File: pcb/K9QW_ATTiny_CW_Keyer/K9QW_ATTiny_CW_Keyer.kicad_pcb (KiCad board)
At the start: 2 copper layers, 13 x 1.4 mm, 25 parts, among them J1 Paddle Input, J2 Key Output, J3 Command, J4 Key LED, J5 Barrel_Jack_MountingPin, J6 Power Input, J7 Paddle Input, J8 Key Output, Q1 MMBT3904, Q2 MMBT3904, SW1 Command, SW2 Power Switch, U1 ATtiny85-20P, U2 LD1117S33TR_SOT223

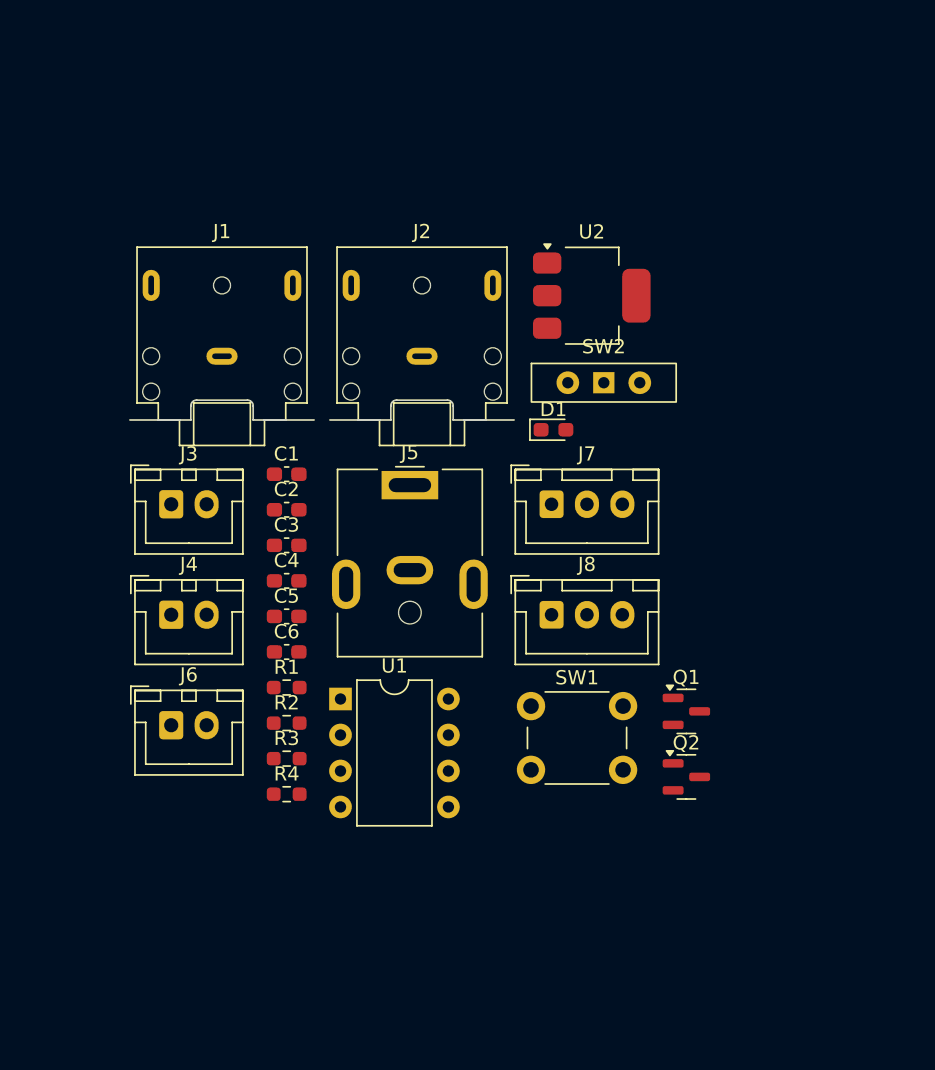
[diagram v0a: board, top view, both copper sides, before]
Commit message: Fixing LED and adding Sidetone Connector
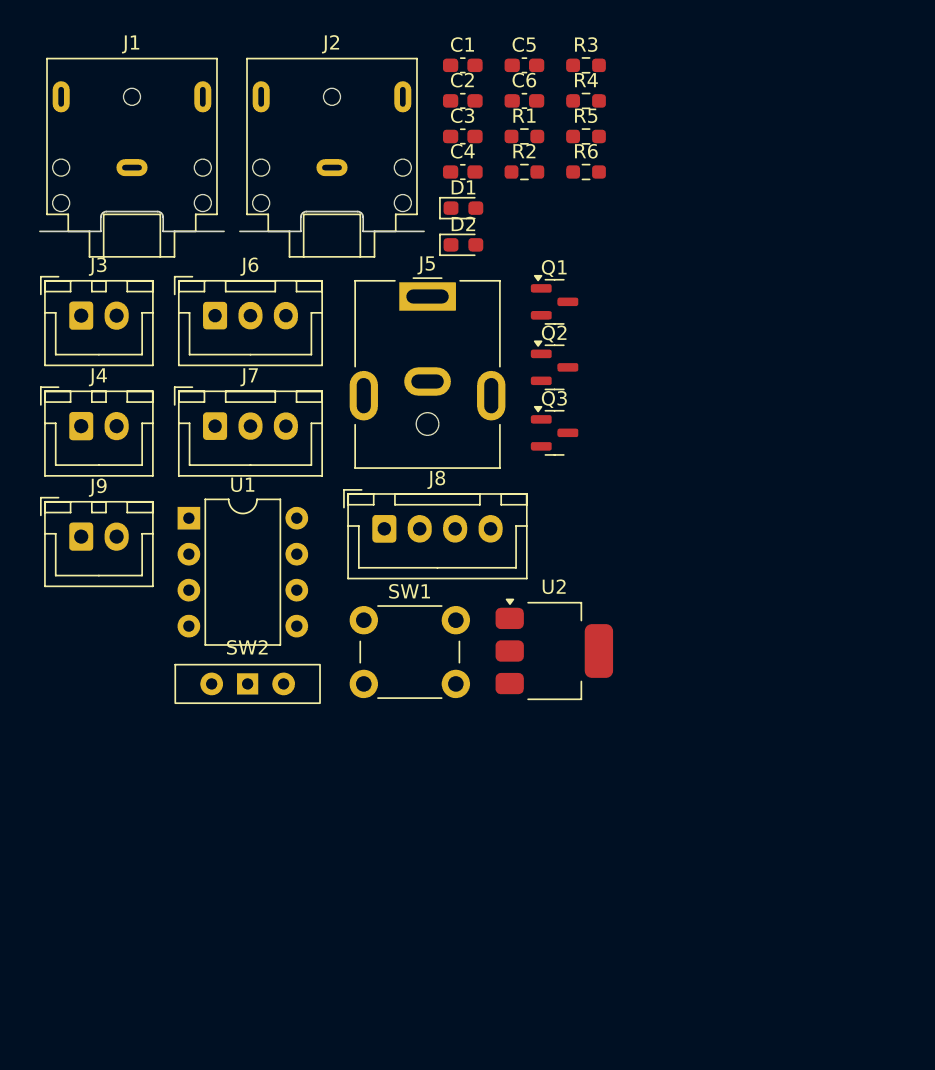
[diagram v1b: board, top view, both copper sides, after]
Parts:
- added D2: Side LED, LED_SMD:LED_0603_1608Metric_Pad1.05x0.95mm_HandSolder, F.Cu at (148.2, 75.0)
- added J9: Power Input, Connector_JST:JST_XH_B2B-XH-A_1x02_P2.50mm_Vertical, F.Cu at (121.2, 95.6)
- added Q3: MMBT3904, Package_TO_SOT_SMD:SOT-23, F.Cu at (154.6, 88.2)
- added R5: 4.7k, Resistor_SMD:R_0603_1608Metric_Pad0.98x0.95mm_HandSolder, F.Cu at (156.8, 67.3)
- added R6: 220, Resistor_SMD:R_0603_1608Metric_Pad0.98x0.95mm_HandSolder, F.Cu at (156.8, 69.8)
- D1: value KEY LED -> LED
- J4: value Key LED -> Sidetone
- J6: value Power Input -> Paddle Input; footprint Connector_JST:JST_XH_B2B-XH-A_1x02_P2.50mm_Vertical -> Connector_JST:JST_XH_B3B-XH-A_1x03_P2.50mm_Vertical
- J7: value Paddle Input -> Key Output
- J8: value Key Output -> LED; footprint Connector_JST:JST_XH_B3B-XH-A_1x03_P2.50mm_Vertical -> Connector_JST:JST_XH_B4B-XH-A_1x04_P2.50mm_Vertical
- Q1: value MMBT3904 -> MMBT2222A
- R3: value 220 -> 4.7k
- R4: value 4.7k -> 220
- moved R4 53.3 mm to (156.8, 64.8)
- moved R3 53.3 mm to (156.8, 62.3)
- moved C6 42.4 mm to (152.5, 64.8)
- moved R1 42.4 mm to (152.5, 67.3)
- moved R2 42.4 mm to (152.5, 69.8)
- moved C5 42.4 mm to (152.5, 62.3)
- moved SW2 32.9 mm to (132.9, 106.0)
- moved C1 31.4 mm to (148.1, 62.3)
- moved C2 31.4 mm to (148.1, 64.8)
- moved C4 31.4 mm to (148.1, 69.8)
- moved C3 31.4 mm to (148.1, 67.3)
- moved Q1 30.4 mm to (154.6, 79.0)
- moved Q2 30.4 mm to (154.6, 83.6)
- moved J6 29.1 mm to (130.6, 80.0)
- moved U2 25.2 mm to (154.6, 103.6)
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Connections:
- D1 pad 1: GND -> Net-(D1-K)
- J4 pad 1: Net-(D1-A) -> SIDETONE
- J6 pad 1: VDC -> GND
- J6 pad 2: GND -> DAH
- J7 pad 2: DAH -> KEY Ring
- J7 pad 3: DIT -> KEY Out
- J8 pad 1: GND -> Net-(D1-A)
- J8 pad 2: KEY Ring -> Net-(D1-K)
- J8 pad 3: KEY Out -> Net-(D2-A)
- Q2 pad 2: Net-(Q2-E) -> GND
- Q2 pad 3: VCC -> Net-(D1-K)
- R3 pad 1: Net-(D1-A) -> KEY
- R3 pad 2: Net-(Q2-E) -> Net-(Q2-B)
- R4 pad 1: KEY -> VCC
- R4 pad 2: Net-(Q2-B) -> Net-(D1-A)

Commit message: Rough PCB Layout
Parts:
- D1: value LED -> Key
- D2: value Side LED -> Sidetone
- moved R3 63.0 mm to (144.1, 124.0), turned to -90 degrees
- moved R5 53.4 mm to (144.1, 119.1), turned to -90 degrees
- moved R4 51.2 mm to (166.2, 115.2), turned to 180 degrees
- moved C1 50.7 mm to (147.4, 113.0)
- moved J1 50.7 mm to (170.5, 91.4), turned to 90 degrees
- moved D2 48.7 mm to (172.5, 117.2), turned to 180 degrees
- moved J2 48.7 mm to (170.5, 106.6), turned to 90 degrees
- moved D1 48.3 mm to (166.2, 117.2), turned to 180 degrees
- moved R6 48.0 mm to (172.5, 115.2)
- moved J3 46.7 mm to (155.9, 111.2), turned to 90 degrees
- moved R1 42.3 mm to (147.8, 109.3), turned to 90 degrees
- moved Q2 40.9 mm to (148.0, 124.0), turned to 90 degrees
- moved SW1 39.7 mm to (172.6, 125.6), turned to 180 degrees
- moved C2 38.7 mm to (138.8, 102.3), turned to 90 degrees
- moved J4 37.5 mm to (155.9, 101.8), turned to 90 degrees
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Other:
- board size 13 x 1.4 mm -> 1.4 x 13 mm

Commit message: Rough routing
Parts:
- moved R4 6.12 mm to (172.4, 115.3), turned to 0 degrees
- moved D1 6.12 mm to (172.3, 117.3), turned to 0 degrees
- moved D2 6.10 mm to (166.4, 117.3), turned to 0 degrees
- moved R6 6.10 mm to (166.4, 115.3), turned to 180 degrees
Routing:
- net VCC: track 0.00 -> 70.6 mm, vias 0 -> 1
- net KEY Out: track 0.00 -> 39.1 mm
- net DIT: track 0.00 -> 37.2 mm
- net COMMAND: track 0.00 -> 37.0 mm
- net DAH: track 0.00 -> 36.1 mm
- net KEY Ring: track 0.00 -> 30.8 mm
- net KEY: track 0.00 -> 30.4 mm
- net SIDETONE: track 0.00 -> 29.3 mm
- net VDC: track 0.00 -> 27.6 mm
- net Net-(D1-K): track 0.00 -> 25.9 mm
- net Net-(D1-A): track 0.00 -> 22.7 mm
- net Net-(D2-K): track 0.00 -> 17.8 mm
- net Net-(D2-A): track 0.00 -> 14.7 mm
- net Net-(SW2-B): track 0.00 -> 11.0 mm
- net Net-(U1-~{RESET}/PB5): track 0.00 -> 5.18 mm
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- added copper zone on B.Cu, net GND
- added copper zone on F.Cu, net GND
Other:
- board size 1.4 x 13 mm -> 57.8 x 45.1 mm

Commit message: Layout cleanup
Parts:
- added JP1: SolderJumper_2_Open, Jumper:SolderJumper-2_P1.3mm_Open_RoundedPad1.0x1.5mm, B.Cu at (134.7, 91.6)
- moved C6 12.8 mm to (134.7, 97.5), turned to -90 degrees
- moved J9 3.61 mm to (129.4, 107.4)
- moved C5 1.85 mm to (136.1, 85.9), turned to 0 degrees
- moved SW2 1.29 mm to (124.9, 87.1)
- moved J1 0.80 mm to (170.9, 90.7)
- moved J5 0.78 mm to (131.0, 96.6)
- moved J2 0.39 mm to (170.9, 106.6)
- moved U2 0.27 mm to (137.5, 91.2)
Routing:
- net Net-(JP1-A): track 11.0 -> 19.0 mm
- net VDC: track 27.6 -> 24.5 mm
- net VCC: track 70.6 -> 69.6 mm
- net DIT: track 37.2 -> 37.9 mm
- net GND: vias 5 -> 8
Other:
- board size 57.8 x 45.1 mm -> 57.1 x 50.8 mm

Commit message: Refining layout
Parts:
- added R7: 50, Resistor_SMD:R_0603_1608Metric_Pad0.98x0.95mm_HandSolder, F.Cu at (120.4, 86.8)
- JP1: moved to F.Cu
- SW2: footprint Button_Switch_THT:SW_Slide-03_Wuerth-WS-SLTV_10x2.5x6.4_P2.54mm -> Connector_JST:JST_XH_B3B-XH-A_1x03_P2.50mm_Vertical
- moved C4 26.3 mm to (129.8, 116.1), turned to 90 degrees
- moved Q1 22.4 mm to (132.8, 116.1), turned to -90 degrees
- moved R2 18.3 mm to (135.4, 116.1), turned to 90 degrees
- moved C6 12.7 mm to (139.9, 85.9), turned to 0 degrees
- moved JP1 8.08 mm to (135.9, 83.6), turned to 0 degrees
- moved J9 6.10 mm to (123.3, 106.9), turned to 0 degrees
- moved C5 1.78 mm to (134.3, 85.9), turned to 180 degrees
- moved R1 1.38 mm to (146.4, 109.2)
- moved SW2 1.33 mm to (124.5, 85.9), turned to 0 degrees
- moved C3 1.29 mm to (142.2, 103.3), turned to 0 degrees
- moved R3 1.04 mm to (145.2, 124.0)
- moved R5 1.04 mm to (145.2, 119.1)
- moved C2 0.07 mm to (138.8, 102.4)
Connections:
- J6 pad 1: GND -> DAH
- J6 pad 2: DAH -> DIT
- J6 pad 3: DIT -> GND
- J7 pad 1: GND -> KEY Ring
- J7 pad 2: KEY Ring -> KEY Out
- J7 pad 3: KEY Out -> GND
- SW2 pad 1: GND -> Net-(SW2-A)
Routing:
- net KEY Out: track 39.5 -> 60.2 mm
- net KEY: track 30.4 -> 18.1 mm
- net VCC: track 69.6 -> 80.3 mm
- net Net-(JP1-A): track 19.0 -> 13.7 mm
- net Net-(SW2-A): track 0.00 -> 4.14 mm
- net DAH: track 36.2 -> 33.7 mm
- net KEY Ring: track 31.1 -> 33.0 mm
- net Net-(U1-~{RESET}/PB5): track 5.18 -> 3.95 mm
- net DIT: track 37.9 -> 36.7 mm
- net VDC: track 24.5 -> 25.7 mm
- net SIDETONE: track 29.3 -> 30.3 mm
- net Net-(Q3-B): track 2.95 -> 1.96 mm
- net Net-(Q2-B): track 2.95 -> 1.98 mm
- net Net-(Q1-B): track 2.16 -> 1.64 mm
- net GND: vias 8 -> 10
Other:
- board size 57.1 x 50.8 mm -> 57.2 x 50.8 mm
- board text added: "ATTiny85 CW Keyer Edward Sandor, K9QW Sandor Laboratories 2024-08 Rev 1 github.com/ewsandor/ATTiny85_CW_Keyer"
- board text added: "Command"
- board text added: "DC Power"
- board text added: "K"
- board text added: "Key Output"
- board text added: "LED"
- board text added: "Paddle Input"
- board text added: "Power Switch"
- board text added: "S"
- board text added: "Sidetone"

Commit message: Refining routing
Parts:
- added J10: Mounting Hole, MountingHole:MountingHole_3.2mm_M3_Pad_TopBottom, F.Cu at (130.9, 115.3)
- added JP2: Bypass Switch, Jumper:SolderJumper-2_P1.3mm_Open_RoundedPad1.0x1.5mm, F.Cu at (132.0, 91.5)
- JP1: value SolderJumper_2_Open -> Bypass Regulator
- moved C4 24.7 mm to (146.4, 97.8), turned to -90 degrees
- moved Q1 21.2 mm to (143.4, 97.7), turned to 90 degrees
- moved R2 18.0 mm to (139.8, 98.7), turned to 0 degrees
- moved J9 13.8 mm to (124.6, 93.1)
- moved C6 12.7 mm to (134.7, 97.4), turned to -90 degrees
- moved C2 11.4 mm to (150.1, 104.0), turned to 0 degrees
- moved C3 8.14 mm to (149.2, 107.4), turned to -90 degrees
- moved C1 7.94 mm to (139.5, 112.6), turned to -90 degrees
- moved J5 6.94 mm to (130.7, 103.5)
- moved U1 4.90 mm to (147.1, 109.1), turned to 180 degrees
- moved R1 3.98 mm to (143.3, 111.6), turned to 0 degrees
- moved R4 0.79 mm to (171.6, 115.4)
- moved D1 0.79 mm to (171.5, 117.4)
- moved D2 0.74 mm to (167.1, 117.4)
- moved R6 0.74 mm to (167.1, 115.4), turned to 0 degrees
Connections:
- C4 pad 2: Net-(Q1-E) -> GND
- Q1 pad 2: Net-(Q1-E) -> GND
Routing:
- net KEY Out: track 60.2 -> 35.5 mm
- net COMMAND: track 37.0 -> 48.8 mm
- net KEY: track 18.1 -> 29.1 mm
- net SIDETONE: track 30.3 -> 37.4 mm
- net DIT: track 36.7 -> 31.2 mm
- net Net-(JP1-A): track 13.7 -> 18.2 mm
- net VDC: track 25.7 -> 28.7 mm
- net DAH: track 33.7 -> 31.5 mm
- net Net-(Q1-E): track 2.03 -> 0.00 mm
- net Net-(D2-A): track 14.7 -> 16.6 mm
- net Net-(D1-A): track 22.7 -> 21.9 mm
- net Net-(D1-K): track 25.9 -> 25.1 mm
- net Net-(D2-K): track 17.8 -> 18.5 mm
- net VCC: track 80.3 -> 79.7 mm, vias 1 -> 2
- net GND: vias 10 -> 8

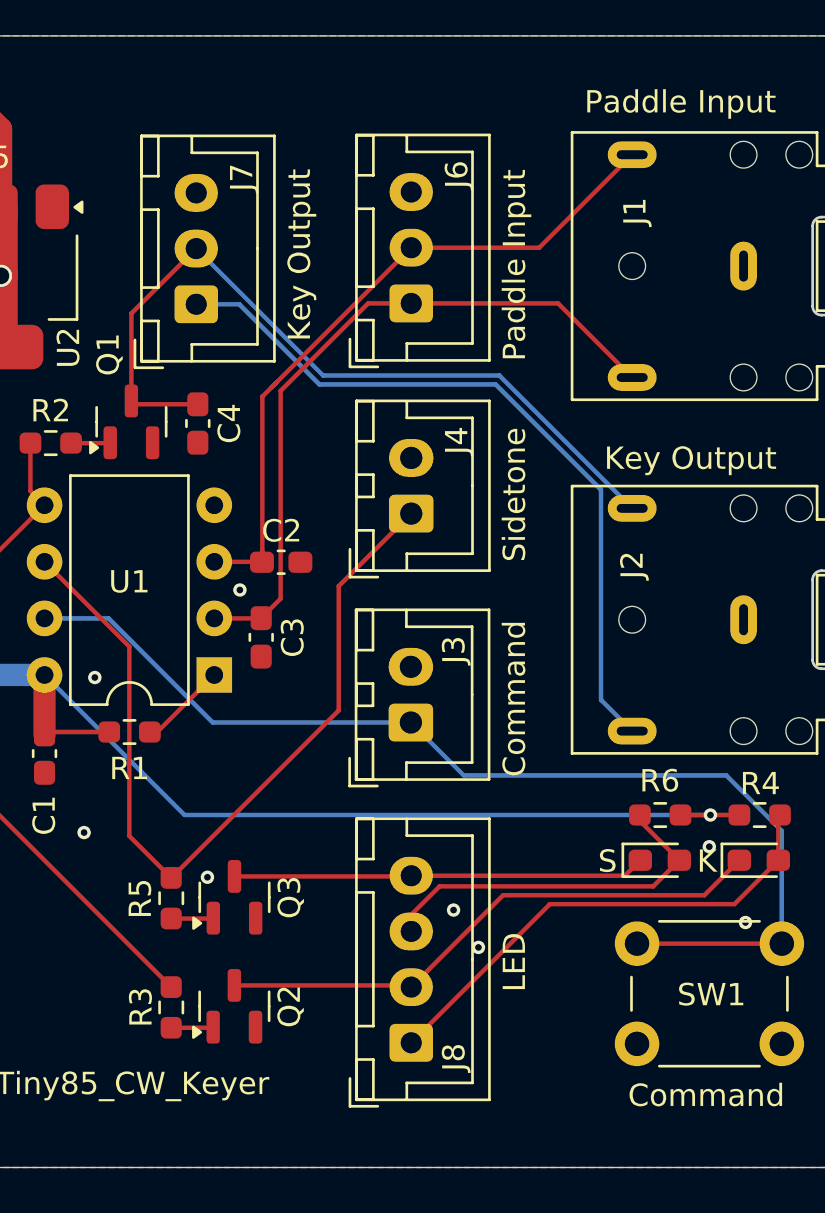
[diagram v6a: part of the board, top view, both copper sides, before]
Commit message: Stripping panel mount headers
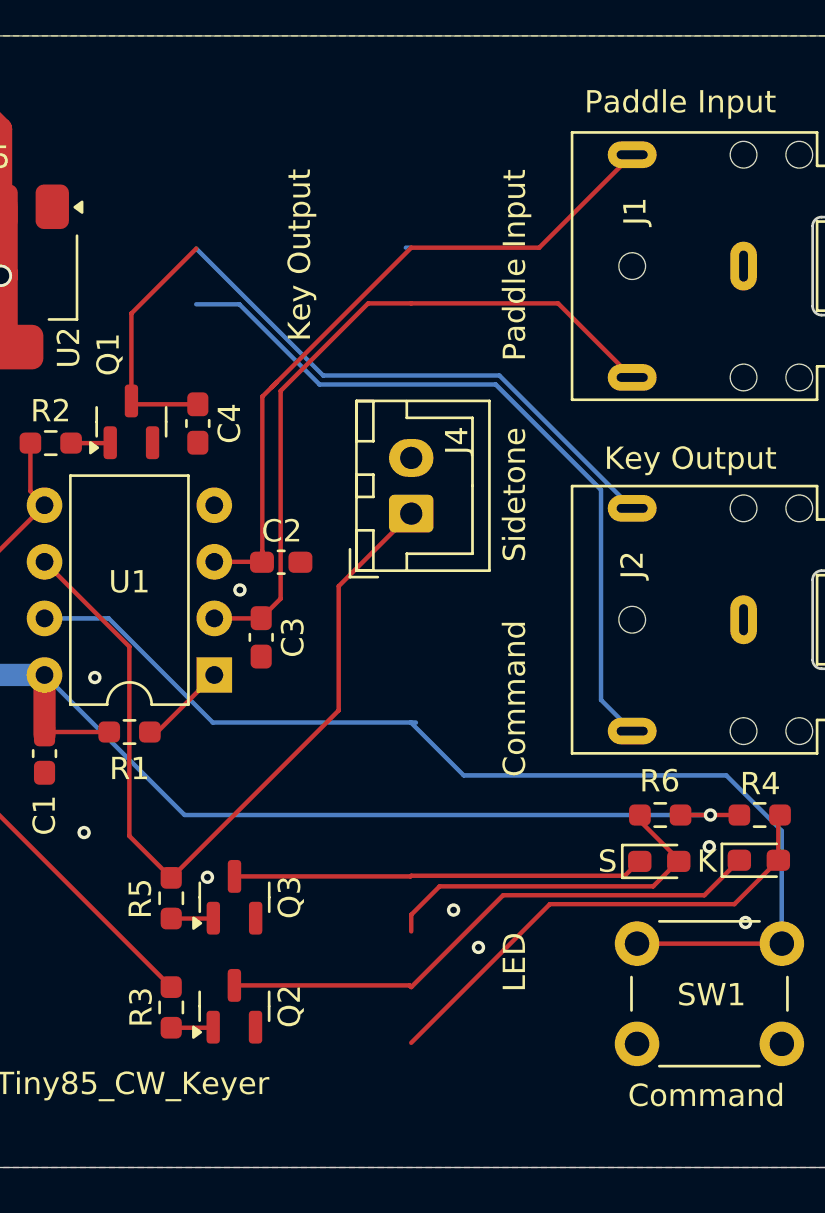
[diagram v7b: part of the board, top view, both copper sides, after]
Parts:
- removed J3: Command, Connector_JST:JST_XH_B2B-XH-A_1x02_P2.50mm_Vertical
- removed J6: Paddle Input, Connector_JST:JST_XH_B3B-XH-A_1x03_P2.50mm_Vertical
- removed J7: Key Output, Connector_JST:JST_XH_B3B-XH-A_1x03_P2.50mm_Vertical
- removed J8: LED, Connector_JST:JST_XH_B4B-XH-A_1x04_P2.50mm_Vertical
- moved D2 0.06 mm to (167.1, 117.4)
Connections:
- SW1 pad 1: GND -> COMMAND
- SW1 pad 2: COMMAND -> GND
